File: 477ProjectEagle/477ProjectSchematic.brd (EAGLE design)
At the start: 101.6 x 127 mm, 69 parts, among them J1 POWER_JACK_BAT, J2 POWER_JACK_12VOUT, Q1 AO4419, X1 22-23-2051, X10 MOTORS, X2 XRJK-S-01-6-6-0-2G2-NO

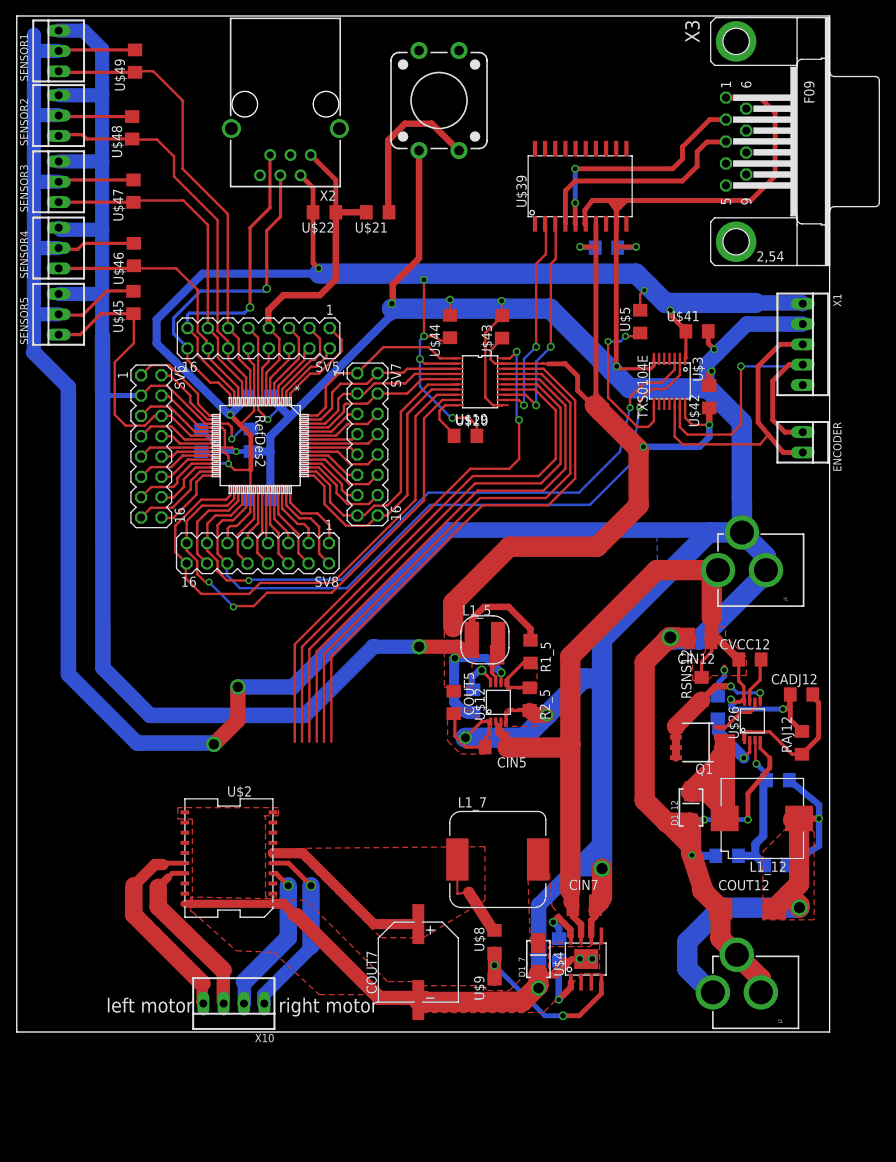
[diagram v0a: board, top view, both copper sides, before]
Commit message: Finished routing everything for main PCB
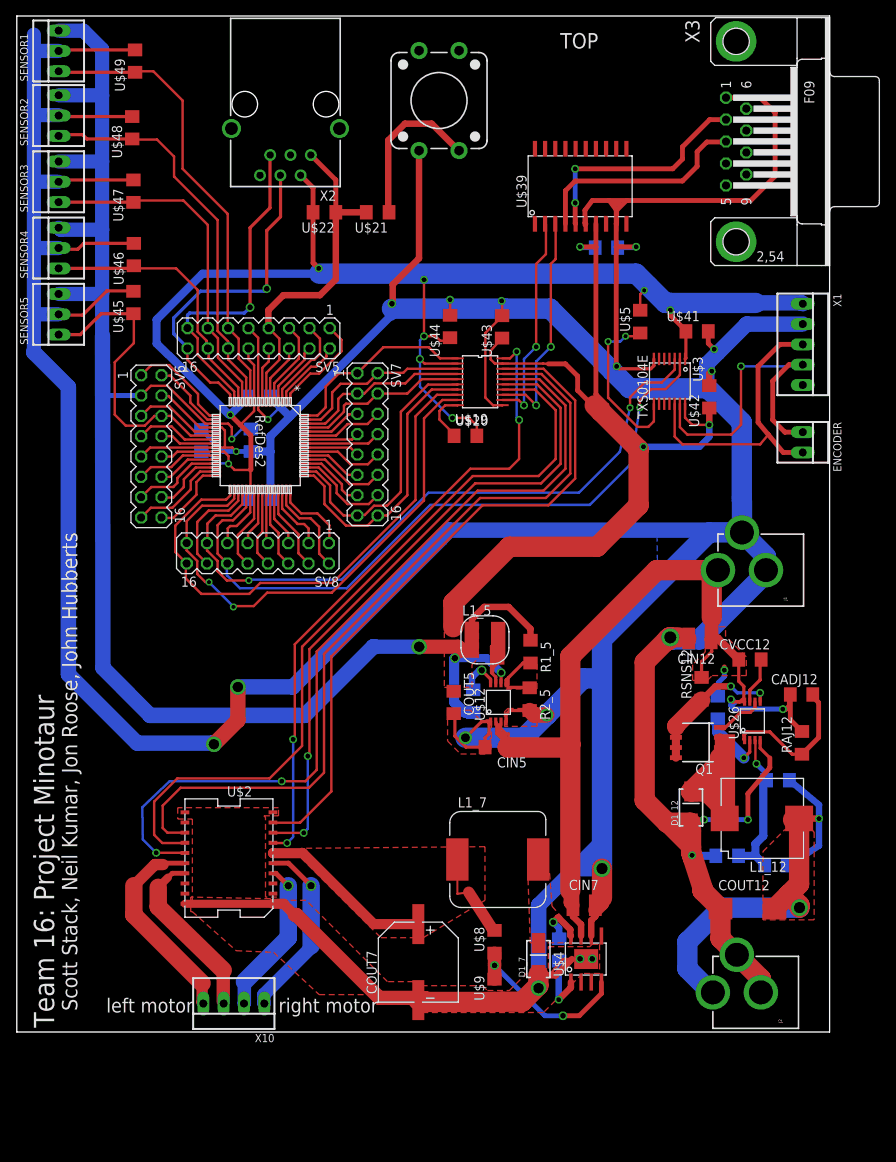
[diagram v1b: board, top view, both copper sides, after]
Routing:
- net N$41: track 69.0 -> 106.2 mm, vias 0 -> 2
- net N$43: track 69.9 -> 101.5 mm
- net N$45: track 67.3 -> 97.6 mm
- net N$44: track 68.2 -> 83.7 mm, vias 0 -> 2
- net N$42: track 70.9 -> 86.0 mm
- net N$39: track 65.5 -> 80.3 mm, vias 2 -> 4
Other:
- board text added: "Scott Stack, Neil Kumar, Jon Roose, John Hubberts"
- board text added: "TOP"
- board text added: "Team 16: Project Minotaur"
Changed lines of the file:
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@@
 <rectangle x1="74.0156" y1="103.6828" x2="76.2" y2="104.2416" layer="1"/>
 <rectangle x1="74.4728" y1="103.1748" x2="75.5396" y2="103.6828" layer="1"/>
+<text x="2.1336" y="42.164" size="2.54" layer="21" rot="R270">Team 16: Project Minotaur</text>
+<text x="67.9196" y="122.936" size="1.9304" layer="21">TOP</text>
+<text x="7.5692" y="2.6416" size="1.9304" layer="21" rot="R90">Scott Stack, Neil Kumar, Jon Roose, John Hubberts</text>
 </plain>
 <attributes>
@@
 <wire x1="61.5696" y1="70.4088" x2="56.6928" y2="70.4088" width="0.3048" layer="1"/>
 <wire x1="56.6928" y1="70.4088" x2="34.7472" y2="48.4632" width="0.3048" layer="1"/>
-<wire x1="34.7472" y1="48.4632" x2="34.7472" y2="36.2712" width="0.3048" layer="1"/>
-<wire x1="32.0176" y1="23.6474" x2="34.7472" y2="36.2712" width="0" layer="19" extent="1-1"/>
+<wire x1="34.7472" y1="48.4632" x2="34.7472" y2="36.7792" width="0.3048" layer="1"/>
+<wire x1="34.7472" y1="36.7792" x2="34.544" y2="36.576" width="0.3048" layer="1"/>
+<via x="34.544" y="36.576" extent="1-16" drill="0.6"/>
+<wire x1="34.544" y1="36.576" x2="34.544" y2="24.384" width="0.3048" layer="16"/>
+<wire x1="34.544" y1="24.384" x2="33.782" y2="23.622" width="0.3048" layer="16"/>
+<via x="33.782" y="23.622" extent="1-16" drill="0.6"/>
+<wire x1="33.782" y1="23.622" x2="32.043" y2="23.622" width="0.3048" layer="1"/>
+<wire x1="32.043" y1="23.622" x2="32.0176" y2="23.6474" width="0.3048" layer="1"/>
 </signal>
 <signal name="N$42">
@@
 <wire x1="32.043" y1="26.2128" x2="32.0176" y2="26.1874" width="0.3048" layer="1"/>
 <wire x1="58.2168" y1="65.8368" x2="39.3192" y2="46.9392" width="0.3048" layer="1"/>
-<wire x1="39.3192" y1="46.9392" x2="39.3192" y2="36.2712" width="0.3048" layer="1"/>
-<wire x1="32.043" y1="26.2128" x2="39.3192" y2="36.2712" width="0" layer="19" extent="1-1"/>
+<wire x1="39.3192" y1="46.9392" x2="39.3192" y2="30.0736" width="0.3048" layer="1"/>
+<wire x1="39.3192" y1="30.0736" x2="35.4076" y2="26.162" width="0.3048" layer="1"/>
+<wire x1="35.4076" y1="26.162" x2="32.043" y2="26.162" width="0.3048" layer="1"/>
+<wire x1="32.043" y1="26.162" x2="32.0176" y2="26.1874" width="0.3048" layer="1"/>
 </signal>
 <signal name="N$43">
@@
 <wire x1="66.1416" y1="66.7512" x2="57.912" y2="66.7512" width="0.3048" layer="1"/>
 <wire x1="57.912" y1="66.7512" x2="38.4048" y2="47.244" width="0.3048" layer="1"/>
-<wire x1="38.4048" y1="47.244" x2="38.4048" y2="36.2712" width="0.3048" layer="1"/>
-<wire x1="21.0176" y1="24.9174" x2="38.4048" y2="36.2712" width="0" layer="19" extent="1-1"/>
+<wire x1="38.4048" y1="47.244" x2="38.4048" y2="32.4104" width="0.3048" layer="1"/>
+<wire x1="21.0176" y1="24.9174" x2="18.8214" y2="24.9174" width="0.3048" layer="1"/>
+<wire x1="18.8214" y1="24.9174" x2="18.2372" y2="25.5016" width="0.3048" layer="1"/>
+<wire x1="18.2372" y1="25.5016" x2="18.2372" y2="28.2956" width="0.3048" layer="1"/>
+<wire x1="18.2372" y1="28.2956" x2="20.4724" y2="30.5308" width="0.3048" layer="1"/>
+<wire x1="20.4724" y1="30.5308" x2="36.5252" y2="30.5308" width="0.3048" layer="1"/>
+<wire x1="36.5252" y1="30.5308" x2="38.4048" y2="32.4104" width="0.3048" layer="1"/>
 </signal>
 <signal name="N$41">
@@
 <wire x1="65.8368" y1="67.6656" x2="57.6072" y2="67.6656" width="0.3048" layer="1"/>
 <wire x1="57.6072" y1="67.6656" x2="37.4904" y2="47.5488" width="0.3048" layer="1"/>
-<wire x1="37.4904" y1="47.5488" x2="37.4904" y2="36.2712" width="0.3048" layer="1"/>
-<wire x1="21.0176" y1="22.3774" x2="37.4904" y2="36.2712" width="0" layer="19" extent="1-1"/>
+<wire x1="37.4904" y1="47.5488" x2="37.4904" y2="32.766" width="0.3048" layer="1"/>
+<wire x1="19.1008" y1="31.3436" x2="15.6972" y2="28.0924" width="0.3048" layer="16"/>
+<wire x1="15.6972" y1="28.0924" x2="15.748" y2="24.0792" width="0.3048" layer="16"/>
+<wire x1="15.748" y1="24.0792" x2="17.4244" y2="22.4028" width="0.3048" layer="16"/>
+<via x="17.4244" y="22.4028" extent="1-16" drill="0.6"/>
+<wire x1="17.4244" y1="22.4028" x2="20.9922" y2="22.4028" width="0.3048" layer="1"/>
+<wire x1="20.9922" y1="22.4028" x2="21.0176" y2="22.3774" width="0.3048" layer="1"/>
+<wire x1="37.4904" y1="32.766" x2="36.068" y2="31.3436" width="0.3048" layer="1"/>
+<wire x1="36.068" y1="31.3436" x2="33.1216" y2="31.3436" width="0.3048" layer="1"/>
+<via x="33.1216" y="31.3436" extent="1-16" drill="0.6"/>
+<wire x1="33.1216" y1="31.3436" x2="19.1008" y2="31.3436" width="0.3048" layer="16"/>
 </signal>
 <signal name="N$44">
@@
 <wire x1="65.532" y1="68.58" x2="57.3024" y2="68.58" width="0.3048" layer="1"/>
 <wire x1="57.3024" y1="68.58" x2="36.576" y2="47.8536" width="0.3048" layer="1"/>
-<wire x1="36.576" y1="47.8536" x2="36.576" y2="36.2712" width="0.3048" layer="1"/>
-<wire x1="32.0938" y1="24.9936" x2="36.576" y2="36.2712" width="0" layer="19" extent="1-1"/>
+<wire x1="36.576" y1="47.8536" x2="36.576" y2="34.6964" width="0.3048" layer="1"/>
+<wire x1="36.576" y1="34.6964" x2="36.3728" y2="34.4932" width="0.3048" layer="1"/>
+<via x="36.3728" y="34.4932" extent="1-16" drill="0.6"/>
+<wire x1="36.3728" y1="34.4932" x2="36.3728" y2="25.4" width="0.3048" layer="16"/>
+<wire x1="36.3728" y1="25.4" x2="35.8648" y2="24.892" width="0.3048" layer="16"/>
+<via x="35.8648" y="24.892" extent="1-16" drill="0.6"/>
+<wire x1="35.8648" y1="24.892" x2="32.043" y2="24.892" width="0.3048" layer="1"/>
+<wire x1="32.043" y1="24.892" x2="32.0176" y2="24.9174" width="0.3048" layer="1"/>
 </signal>
 <signal name="N$45">
@@
 <wire x1="65.2272" y1="69.4944" x2="56.9976" y2="69.4944" width="0.3048" layer="1"/>
 <wire x1="56.9976" y1="69.4944" x2="35.6616" y2="48.1584" width="0.3048" layer="1"/>
-<wire x1="35.6616" y1="48.1584" x2="35.6616" y2="36.2712" width="0.3048" layer="1"/>
-<wire x1="21.0176" y1="23.6474" x2="35.6616" y2="36.2712" width="0" layer="19" extent="1-1"/>
+<wire x1="35.6616" y1="48.1584" x2="35.6616" y2="35.7632" width="0.3048" layer="1"/>
+<wire x1="35.6616" y1="35.7632" x2="31.5976" y2="31.6992" width="0.3048" layer="1"/>
+<wire x1="31.5976" y1="31.6992" x2="20.066" y2="31.6992" width="0.3048" layer="1"/>
+<wire x1="20.066" y1="31.6992" x2="17.1704" y2="28.8036" width="0.3048" layer="1"/>
+<wire x1="17.1704" y1="28.8036" x2="17.1704" y2="24.638" width="0.3048" layer="1"/>
+<wire x1="17.1704" y1="24.638" x2="18.1864" y2="23.622" width="0.3048" layer="1"/>
+<wire x1="18.1864" y1="23.622" x2="20.9922" y2="23.622" width="0.3048" layer="1"/>
+<wire x1="20.9922" y1="23.622" x2="21.0176" y2="23.6474" width="0.3048" layer="1"/>
 </signal>
 <signal name="N$47">

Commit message: Scott Lab - PCB All connected
Added kickback diodes to the HBridge circuit. Added power LED and status
LED. Changed all external connectors to parts from the sparkfun library
(DB9, barrel, RJ11). Need to add more silkscreen - label all
connectionsto outside
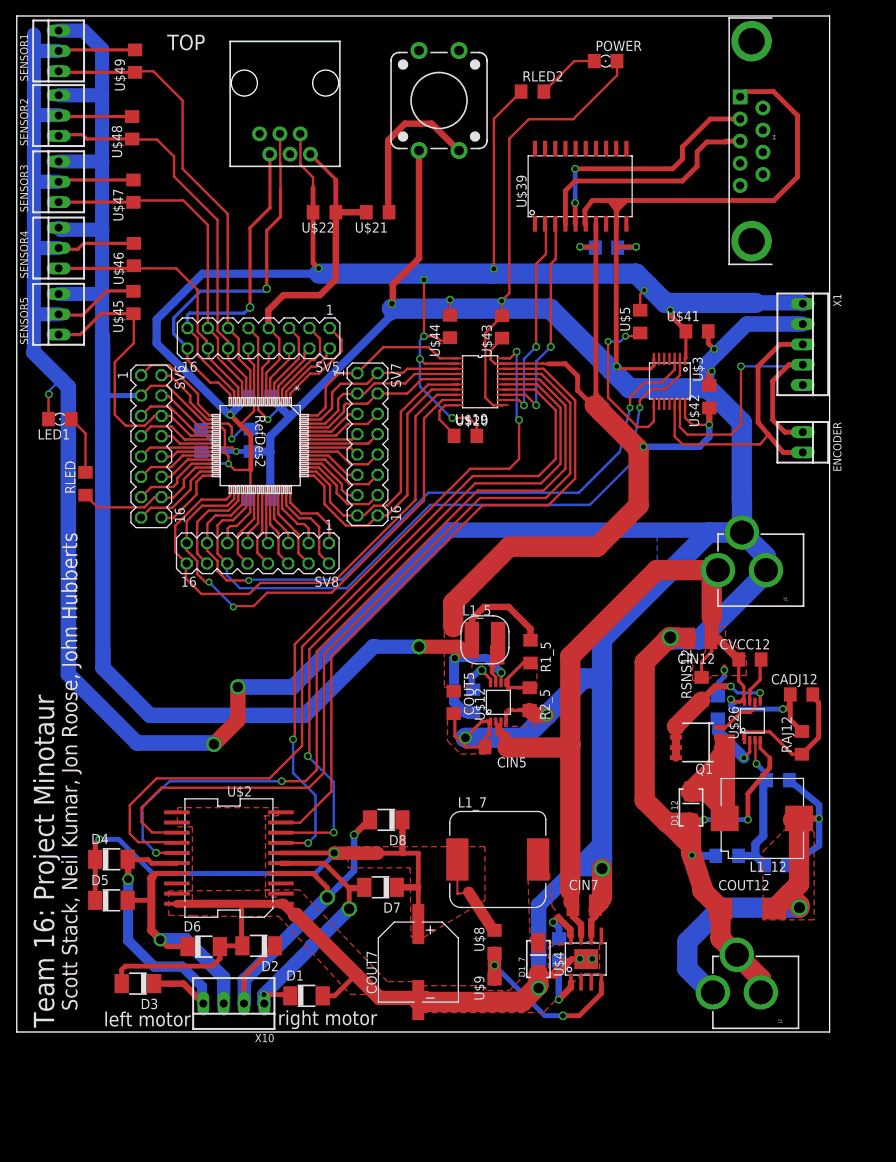
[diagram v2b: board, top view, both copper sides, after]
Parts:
- removed X2: XRJK-S-01-6-6-0-2G2-NO, con-xmultiple:XRJK-S-01-6-6-0-2G2-NO
- removed X3: (no value), con-subd:F09HP
- added D1, D2, D3, D4, D5, D6, D7, D8: (no value), diode:DO-214AC
- added J3: RJ11-6PTH, SparkFun-Connectors:RJ11-6
- added LED1, POWER: (no value), led:1206
- added RLED, RLED2: 1k, MinotaurParts:R1206
- added X4: (no value), SparkFun-Connectors:DB9
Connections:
- new net N$31: LED1.A, RLED.2
- new net N$78: POWER.A, RLED2.2
- net +3V3: now also J3.2, RLED2.1; no longer X2.2
- net +7V: now also D4.C, D5.C, D7.C, D8.C
- net GND: now also D1.A, D2.A, D3.A, D6.A, LED1.C, POWER.C, U$2.SA, U$2.SB, X4.1; no longer X3.1
- net N$14: now also J3.5; no longer X2.5
- net N$18: now also D2.C, D8.A
- net N$19: now also D1.C, D7.A
- net N$20: now also D5.A, D6.C
- net N$21: now also D3.C, D4.A
- net N$30: now also J3.1; no longer X2.1
- net N$53: now also X4.2; no longer X3.2
- net N$66: now also RLED.1
- net N$7: now also J3.4; no longer X2.4
- net N$86: now also J3.3; no longer X2.3
- net N$87: now also X4.3; no longer X3.3
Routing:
- net GND: track 844.0 -> 923.6 mm, vias 20 -> 21
- net +7V: track 33.4 -> 85.0 mm, vias 0 -> 2
- net +3V3: track 220.8 -> 250.2 mm, vias 10 -> 11
- net N$18: track 19.6 -> 46.8 mm, vias 1 -> 2
- net N$19: track 23.1 -> 35.1 mm, vias 1 -> 2
- net N$21: track 25.9 -> 37.5 mm, vias 0 -> 1
- net N$66: track 8.87 -> 19.6 mm
- net N$20: track 22.0 -> 31.5 mm, vias 0 -> 1
- net N$78: track 0.00 -> 7.88 mm
- net N$31: track 0.00 -> 7.39 mm
- net N$45: track 97.6 -> 104.0 mm
- net N$44: track 83.7 -> 89.3 mm
- net N$39: track 80.3 -> 85.9 mm
- net N$7: track 41.9 -> 47.2 mm
- net N$43: track 101.5 -> 106.3 mm
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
